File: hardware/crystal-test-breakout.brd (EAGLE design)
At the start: 29 x 17.8 mm, 11 parts, among them Q1 1N3904

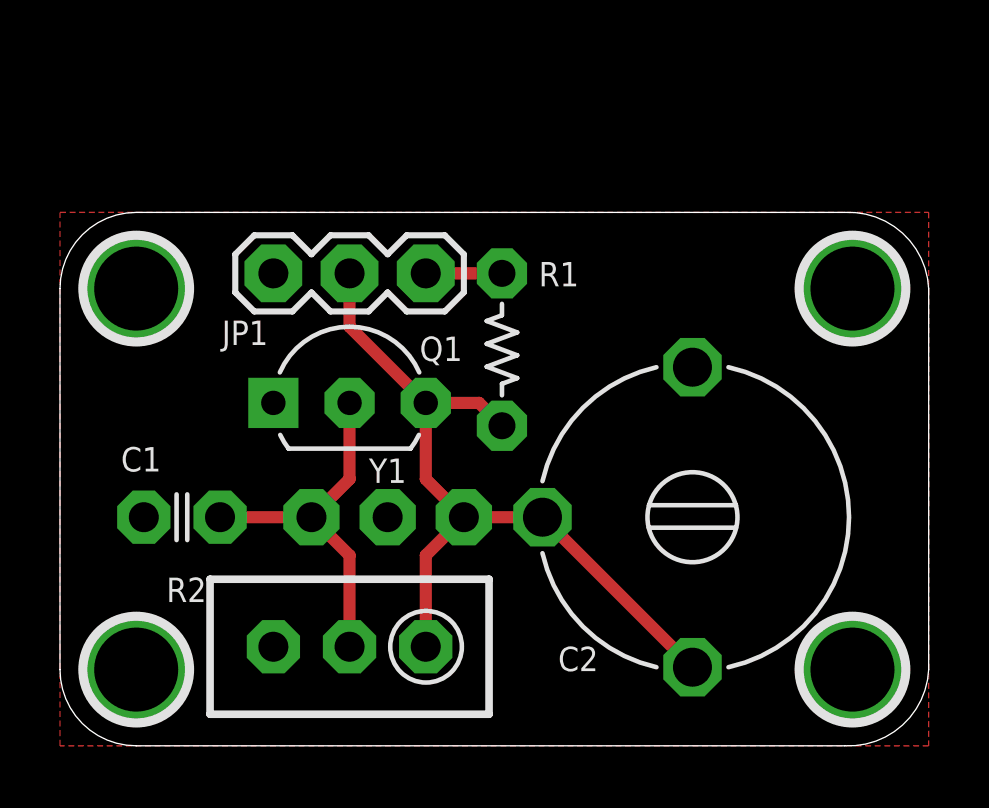
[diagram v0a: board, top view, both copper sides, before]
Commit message: putting trimpot on its side for less whoopsy-daisy factor
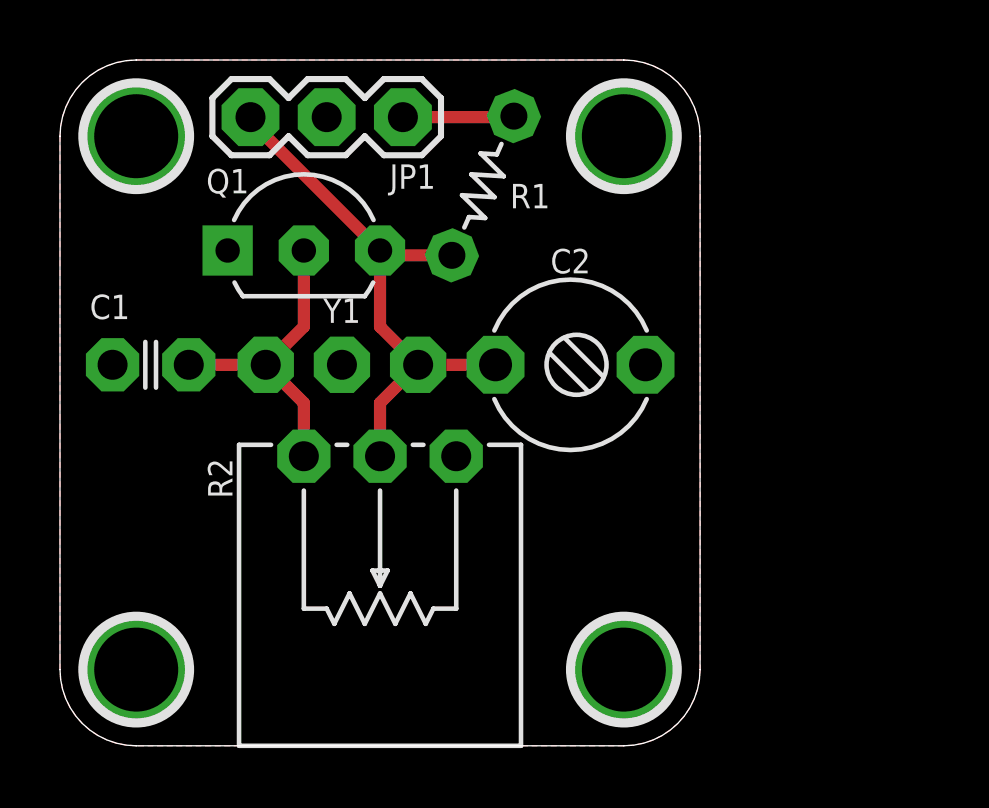
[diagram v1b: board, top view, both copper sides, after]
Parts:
- C2: device A_butts:GYC40000 -> A_butts:CTRIM3050.504
- R2: device A_butts:RTRIM3296W -> A_butts:RTRIM3296W-SIDEWAYS
- moved H2 9.16 mm to (18.8, 20.3)
- moved H4 7.62 mm to (18.8, 2.54)
- moved C2 6.51 mm to (17.0, 12.7), turned to 0 degrees
- moved R2 6.43 mm to (10.7, 9.65)
- moved R1 5.50 mm to (14.1, 18.7), turned to 66 degrees
- moved Q1 5.30 mm to (8.13, 16.5)
- moved Y1 5.30 mm to (9.40, 12.7)
- moved JP1 5.26 mm to (11.4, 21.0)
- moved C1 5.19 mm to (3.02, 12.7)
- moved H1 5.08 mm to (2.54, 20.3)
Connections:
- net GND: now also C2.2, JP1.2; no longer C2.P$1, JP1.3
- net N$1: now also R2.3; no longer R2.2
- net N$4: now also C2.1, JP1.3, R2.2; no longer C2.P$2, C2.P$3, JP1.2, R2.1
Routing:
- net N$4: track 27.1 -> 19.3 mm
- net N$1: track 12.2 -> 10.5 mm
- net VCC: track 2.54 -> 3.71 mm
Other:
- board size 29 x 17.8 mm -> 21.3 x 22.9 mm
